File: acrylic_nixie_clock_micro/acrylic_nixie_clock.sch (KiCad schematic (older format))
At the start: 23 parts, among them IC1 OPT3001DNPR, J1 USB_B_Micro, J2 AVR-ISP-6, Q1 S9013, U1 ATmega328P-AU, U2 AMS1117-3.3v, U3 RX-8025T-UB, Y1 X322516MLB4SI

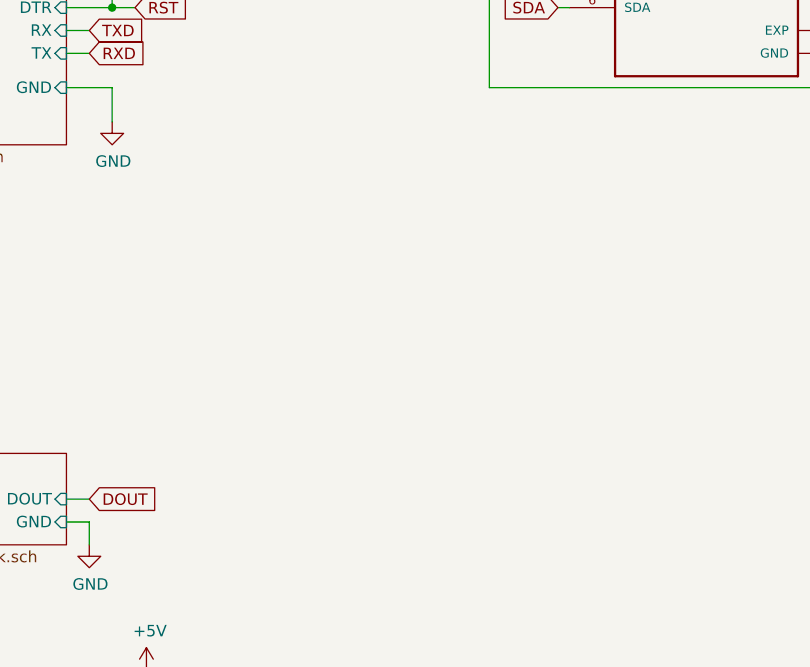
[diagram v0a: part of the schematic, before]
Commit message: 問題点を修正
CH304Gの電源電圧を3.3Vに
RSTにコンデンサを追加
USBのフットプリントを修正
カードコネクタの追加
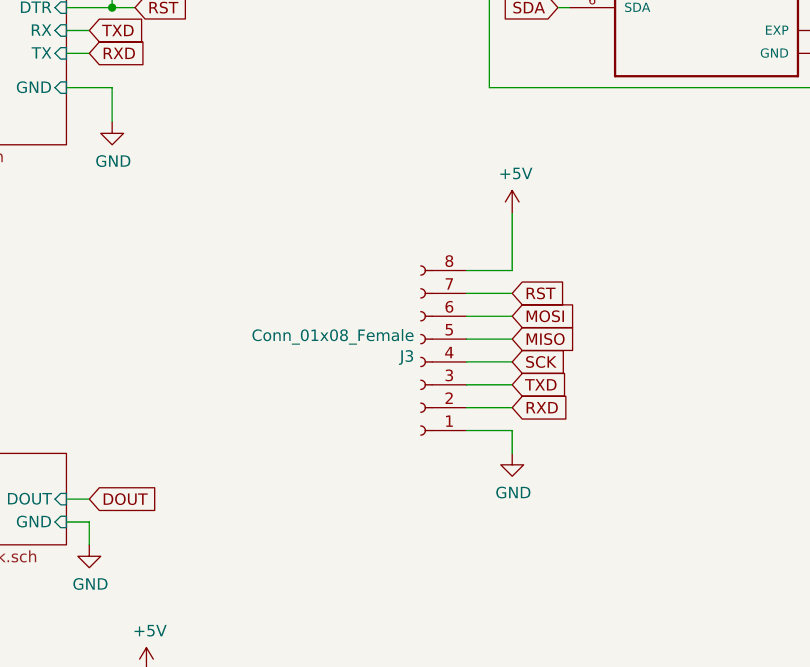
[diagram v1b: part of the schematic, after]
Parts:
- added J3: Conn_01x08_Female, write_card:writer_card, symbol Connector:Conn_01x08_Female
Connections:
- net +5V: now also J3.8 (Pin_8)
- net GND: now also J3.1 (Pin_1)
- net MISO: now also J3.5 (Pin_5)
- net MOSI: now also J3.6 (Pin_6)
- net RST: now also J3.7 (Pin_7)
- net RXD: now also J3.2 (Pin_2)
- net SCK: now also J3.4 (Pin_4)
- net TXD: now also J3.3 (Pin_3)
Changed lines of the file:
@@
 	0    1    1    0
 $EndComp
+$Comp
+L Connector:Conn_01x08_Female J3
+U 1 1 5F83466F
+P 8200 3150
+F 0 "J3" H 8228 3126 50  0000 L CNN
+F 1 "Conn_01x08_Female" H 8228 3035 50  0000 L CNN
+F 2 "write_card:writer_card" H 8200 3150 50  0001 C CNN
+F 3 "~" H 8200 3150 50  0001 C CNN
+	1    8200 3150
+	-1   0    0    1
+$EndComp
+$Comp
+L power:GND #PWR?
+U 1 1 5F83748C
+P 8600 3550
+AR Path="/5E92CCE6/5F83748C" Ref="#PWR?"  Part="1"
+AR Path="/5F83748C" Ref="#PWR026"  Part="1"
+AR Path="/5EA17FAE/5F83748C" Ref="#PWR?"  Part="1"
+AR Path="/5FA639E8/5F83748C" Ref="#PWR?"  Part="1"
+F 0 "#PWR026" H 8600 3300 50  0001 C CNN
+F 1 "GND" H 8605 3377 50  0000 C CNN
+F 2 "" H 8600 3550 50  0001 C CNN
+F 3 "" H 8600 3550 50  0001 C CNN
+	1    8600 3550
+	1    0    0    -1
+$EndComp
+Wire Wire Line
+	8600 3450 8600 3550
+Text GLabel 8600 2850 2    50   Input ~ 0
+RST
+Wire Wire Line
+	8600 2500 8600 2750
+$Comp
+L power:+5V #PWR025
+U 1 1 5F8628DB
+P 8600 2500
+F 0 "#PWR025" H 8600 2350 50  0001 C CNN
+F 1 "+5V" H 8615 2673 50  0000 C CNN
+F 2 "" H 8600 2500 50  0001 C CNN
+F 3 "" H 8600 2500 50  0001 C CNN
+	1    8600 2500
+	1    0    0    -1
+$EndComp
+Text GLabel 8600 3150 2    50   Input ~ 0
+SCK
+Text GLabel 8600 3050 2    50   Input ~ 0
+MISO
+Text GLabel 8600 2950 2    50   Input ~ 0
+MOSI
+Text GLabel 8600 3350 2    50   Input ~ 0
+RXD
+Text GLabel 8600 3250 2    50   Input ~ 0
+TXD
+Wire Wire Line
+	8600 2850 8400 2850
+Wire Wire Line
+	8400 2950 8600 2950
+Wire Wire Line
+	8600 3050 8400 3050
+Wire Wire Line
+	8400 3150 8600 3150
+Wire Wire Line
+	8600 3250 8400 3250
+Wire Wire Line
+	8400 3350 8600 3350
+Wire Wire Line
+	8600 3450 8400 3450
+Wire Wire Line
+	8400 2750 8600 2750
 $EndSCHEMATC
